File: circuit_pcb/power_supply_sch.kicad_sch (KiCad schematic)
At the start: 16 parts, among them IC1 AP7312-1833W6-7

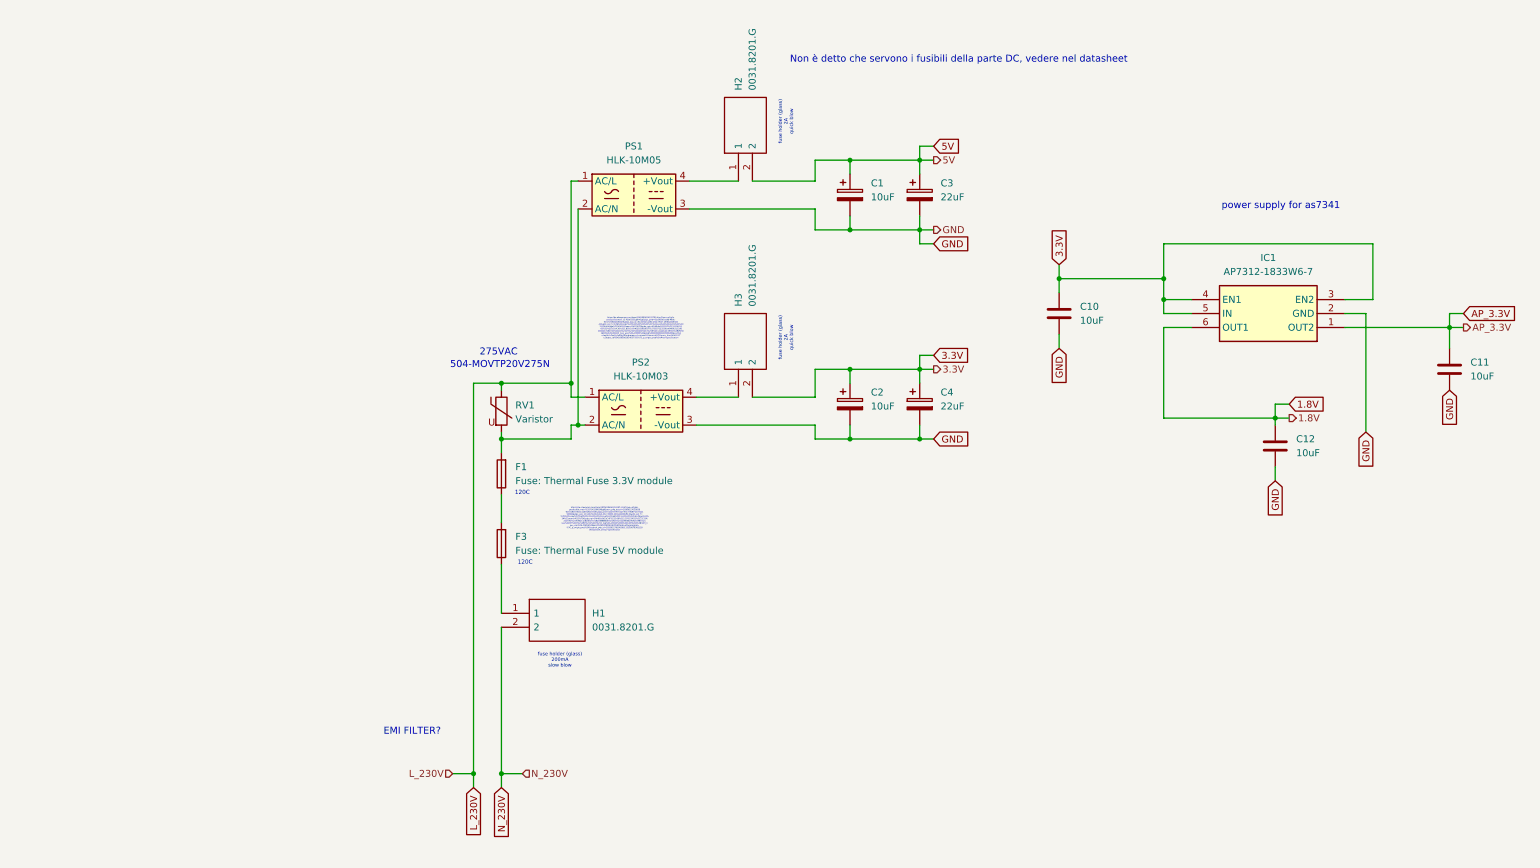
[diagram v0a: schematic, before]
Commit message: [new] circuit pcb: added PMS7003
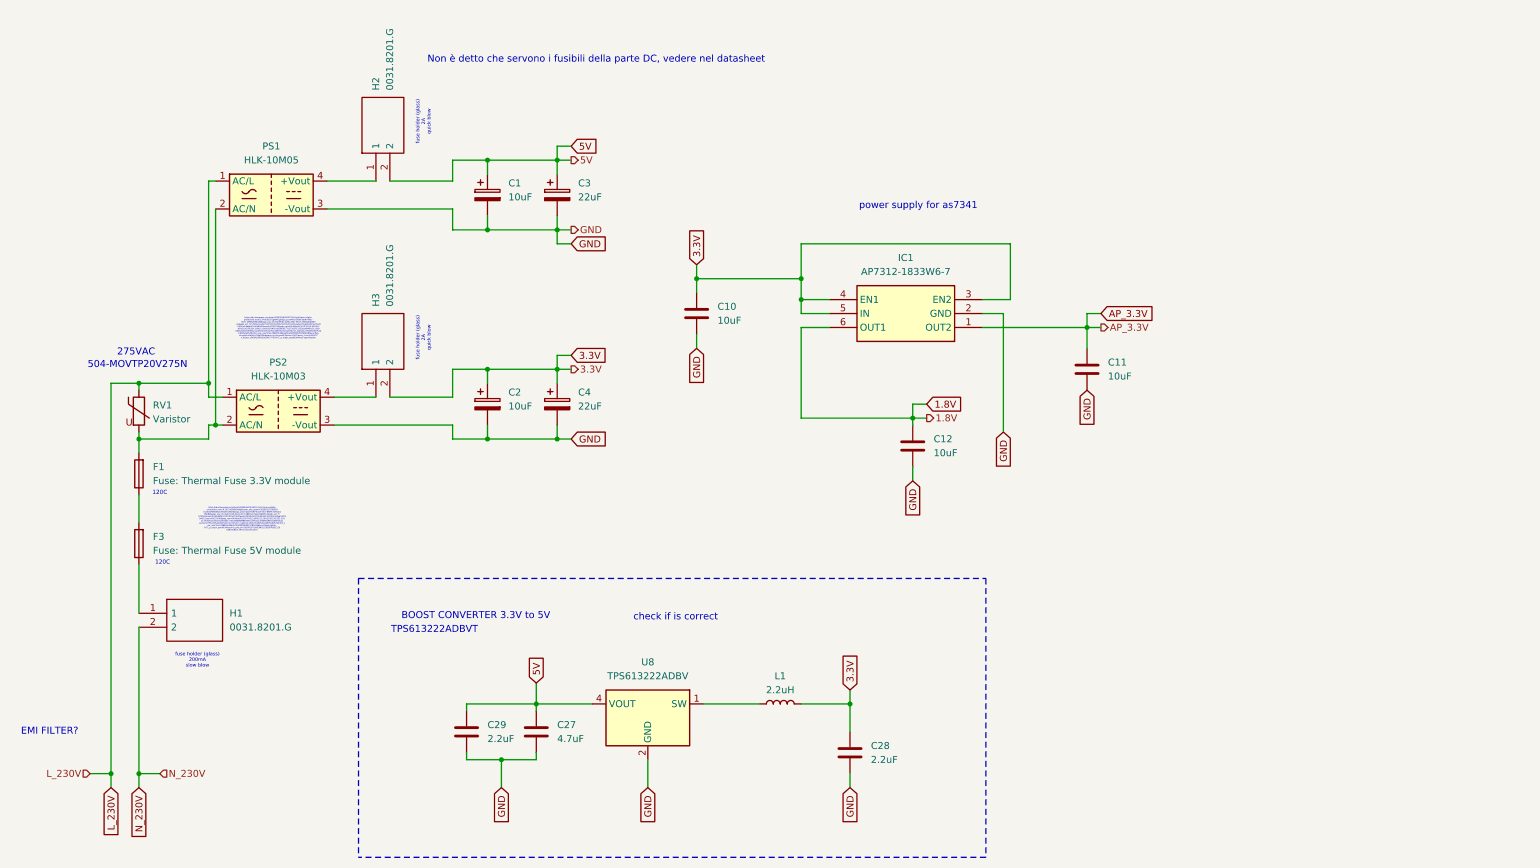
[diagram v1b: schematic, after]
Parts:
- added C27: 4.7uF, symbol Device:C
- added C28, C29: 2.2uF, symbol Device:C
- added L1: 2.2uH, symbol Device:L
- added U8: TPS613222ADBV, Package_TO_SOT_SMD:SOT-23-5, symbol Regulator_Switching:TPS613222ADBV
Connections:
- net 3.3V: now also C28.1, L1.2
- net 5V: now also C27.1, C29.1, U8.4 (VOUT)
- net GND: now also C27.2, C28.2, C29.2, U8.2 (GND)
- new net: L1.1, U8.1 (SW)
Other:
- note added: "BOOST CONVERTER 3.3V to 5V"
- note added: "TPS613222ADBVT"
- note added: "check if is correct"
- moved on the sheet: C1, C10, C11, C12, C2, C3, C4, F1, F3, H1, H2, H3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
